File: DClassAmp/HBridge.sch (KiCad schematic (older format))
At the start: 15 parts

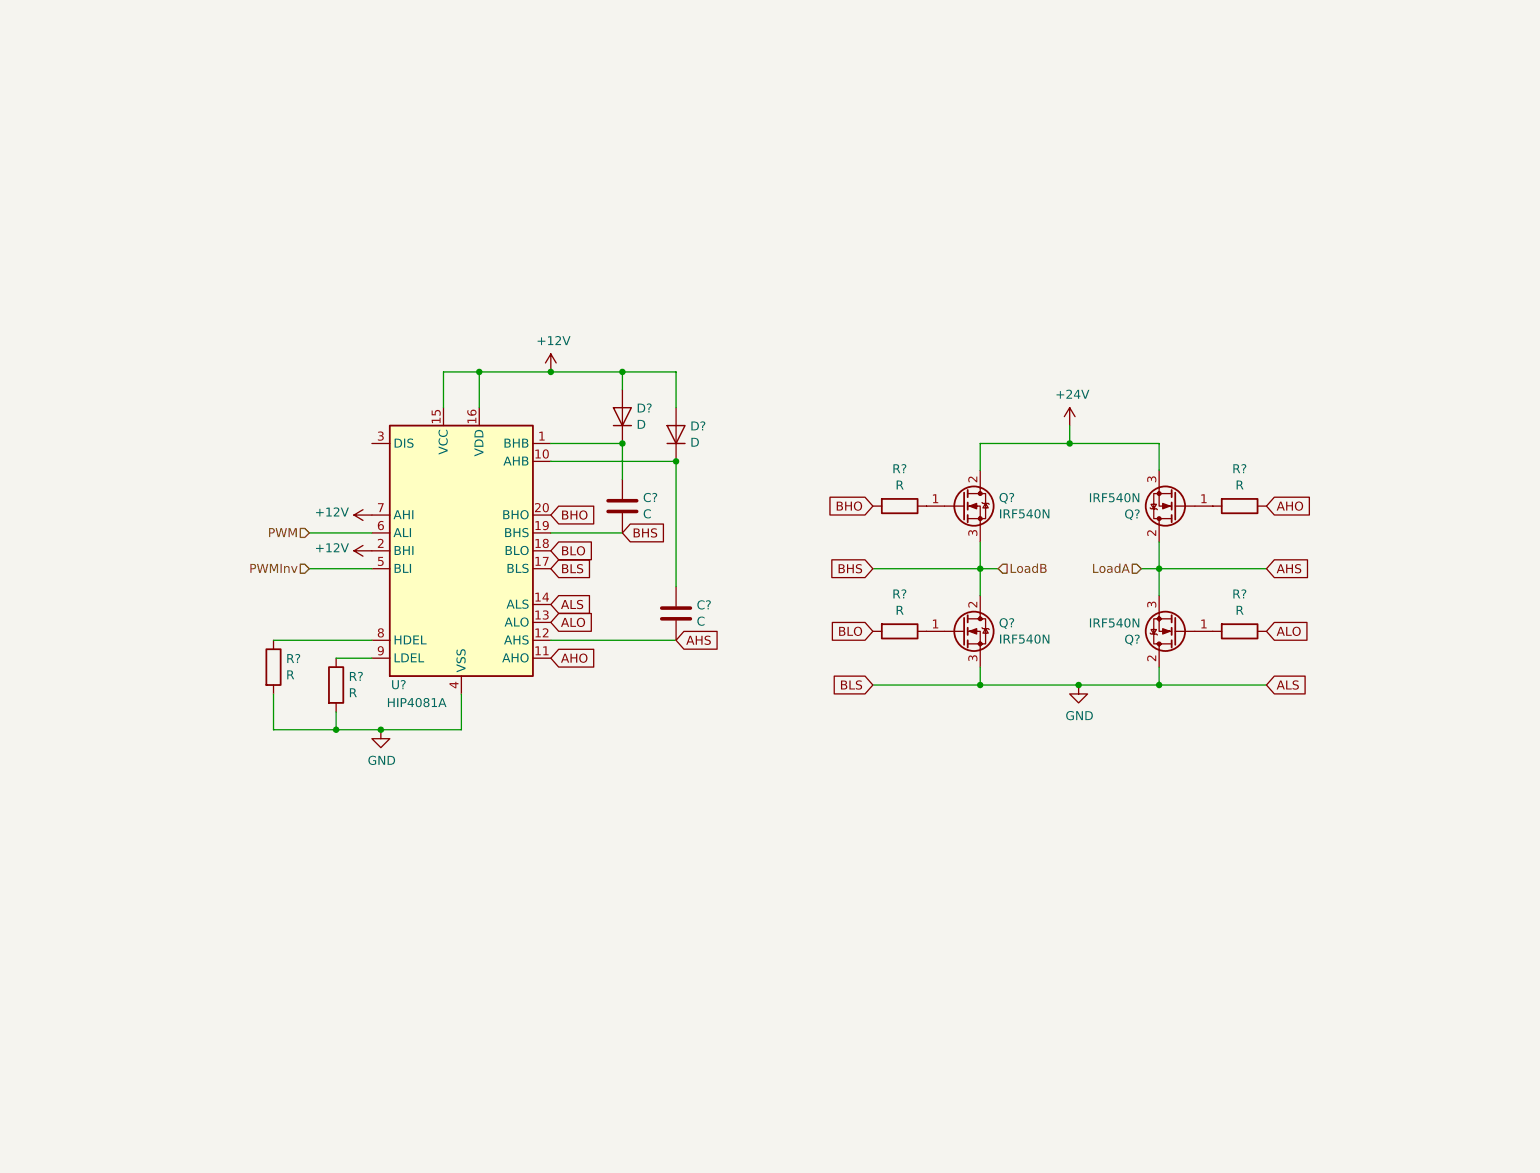
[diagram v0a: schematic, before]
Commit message: Added h bridge v2
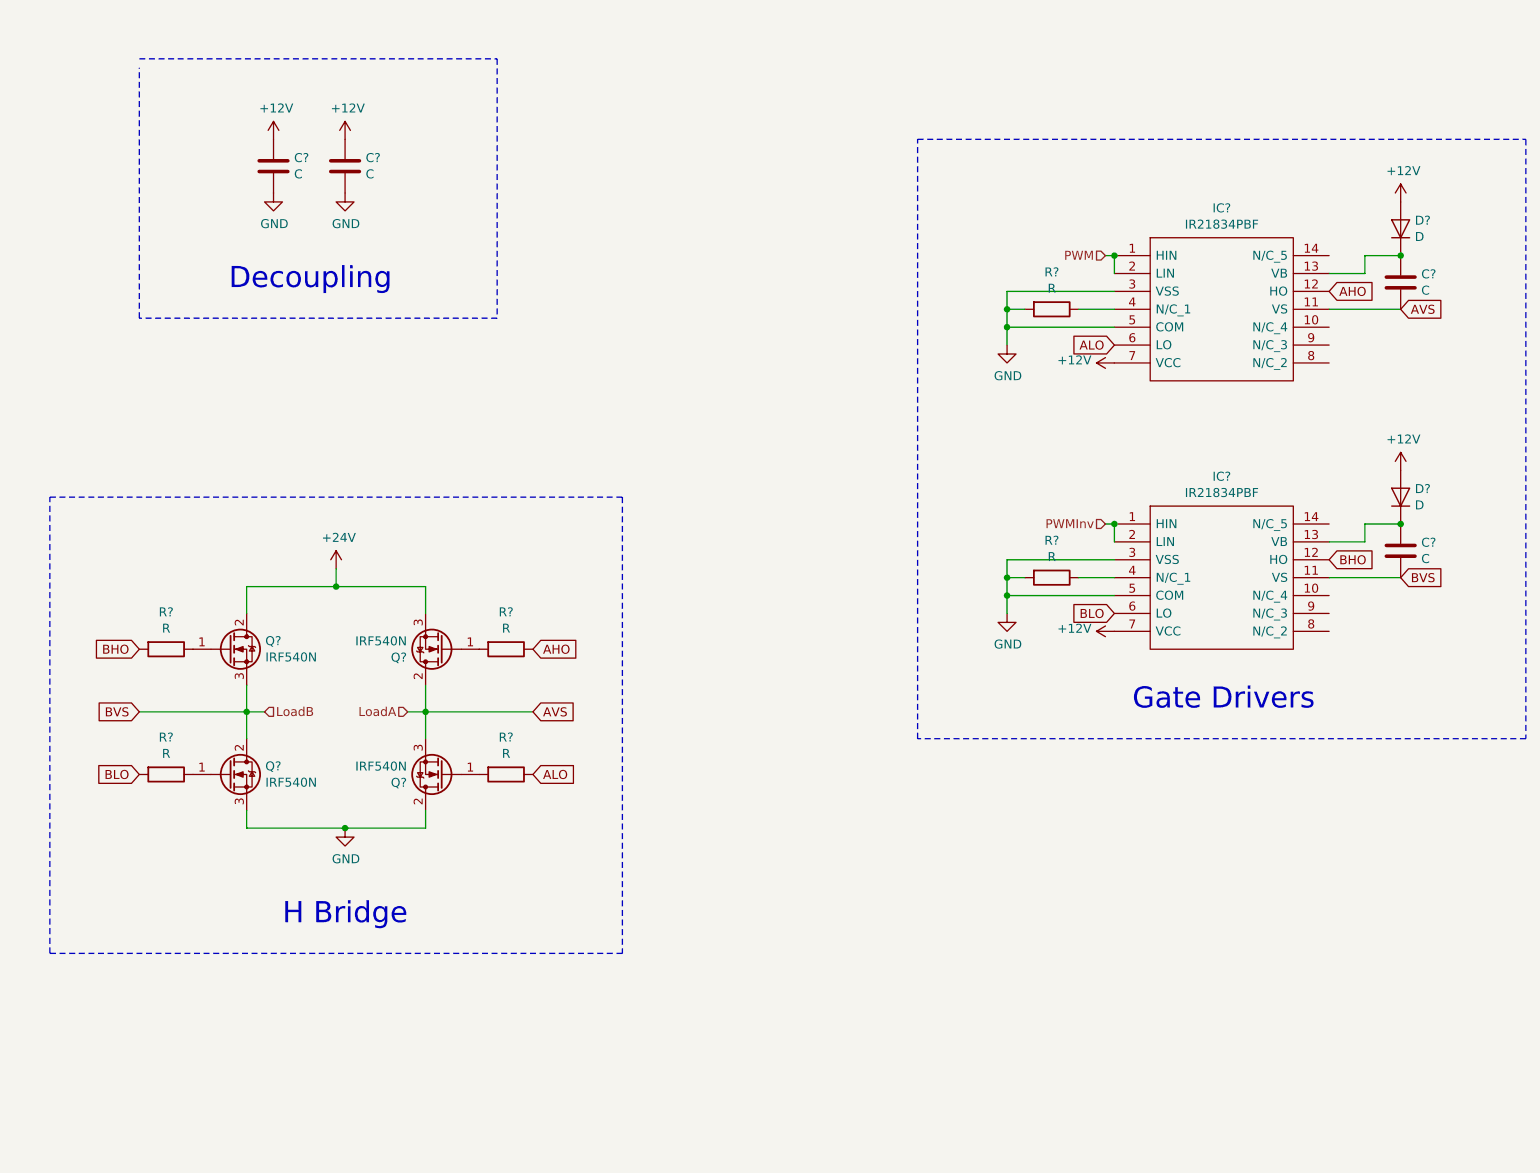
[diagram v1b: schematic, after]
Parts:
- removed C? (x2): C, symbol Device:C
- removed D? (x2): D, symbol Device:D
- removed R? (x2): R, symbol Device:R
- removed U?: HIP4081A, symbol Driver_FET:HIP4081A
- added C? (x4): C, symbol Device:C
- added D? (x2): D, symbol Device:D
- added IC? (x2): IR21834PBF, DIP762W56P254L1930H533Q14N, symbol IR21834PBF:IR21834PBF
- added R? (x2): R, symbol Device:R
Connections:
- net +12V: now also C?.1, C?.1, D?.2 (A), D?.2 (A), IC?.7 (VCC), IC?.7 (VCC)
- net AHO: now also IC?.12 (HO)
- net ALO: now also IC?.6 (LO)
- net BHO: now also IC?.12 (HO)
- net BLO: now also IC?.6 (LO)
- net GND: now also C?.2, C?.2, IC?.3 (VSS), IC?.3 (VSS), IC?.5 (COM), IC?.5 (COM), R?.2, R?.2
- net PWM: now also IC?.1 (HIN), IC?.2 (LIN)
- net PWMInv: now also IC?.1 (HIN), IC?.2 (LIN)
- net AHS renamed AVS
- net AVS: now also C?.2, IC?.11 (VS)
- net BHS renamed BVS
- net BVS: now also C?.2, IC?.11 (VS)
- new net: C?.1, D?.1 (K), IC?.13 (VB) (x2)
- new net: IC?.4 (N/C_1), R?.1 (x2)
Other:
- note added: "Decoupling"
- note added: "Gate Drivers"
- note added: "H Bridge"
- moved on the sheet: Q?, R?

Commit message: Added connector to h bridge schematic
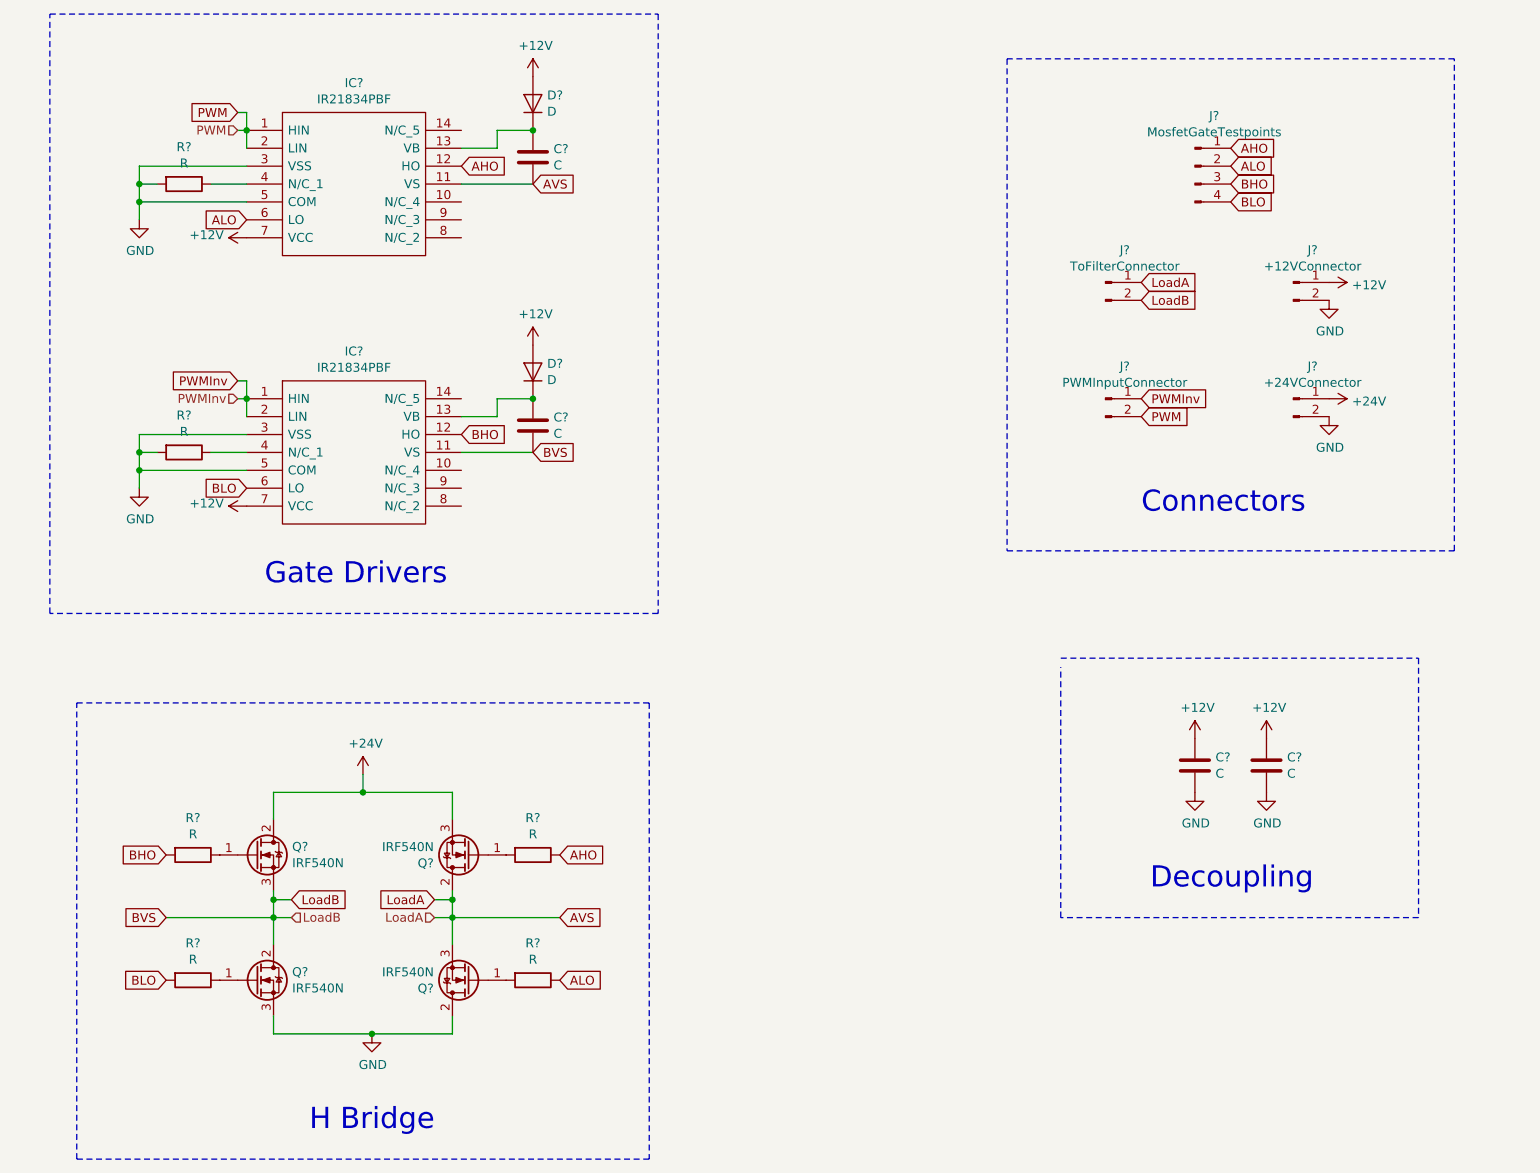
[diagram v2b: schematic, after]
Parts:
- added J?: +12VConnector, symbol Connector:Conn_01x02_Male
- added J?: +24VConnector, symbol Connector:Conn_01x02_Male
- added J?: ToFilterConnector, symbol Connector:Conn_01x02_Male
- added J?: PWMInputConnector, symbol Connector:Conn_01x02_Male
- added J?: MosfetGateTestpoints, symbol Connector:Conn_01x04_Male
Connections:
- net +12V: now also J?.1 (Pin_1)
- net +24V: now also J?.1 (Pin_1)
- net AHO: now also J?.1 (Pin_1)
- net ALO: now also J?.2 (Pin_2)
- net AVS: now also J?.1 (Pin_1)
- net BHO: now also J?.3 (Pin_3)
- net BLO: now also J?.4 (Pin_4)
- net BVS: now also J?.2 (Pin_2)
- net GND: now also J?.2 (Pin_2), J?.2 (Pin_2)
- net PWM: now also J?.2 (Pin_2)
- net PWMInv: now also J?.1 (Pin_1)
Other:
- note added: "Connectors"
- moved on the sheet: C?, D?, IC?, Q?, R?

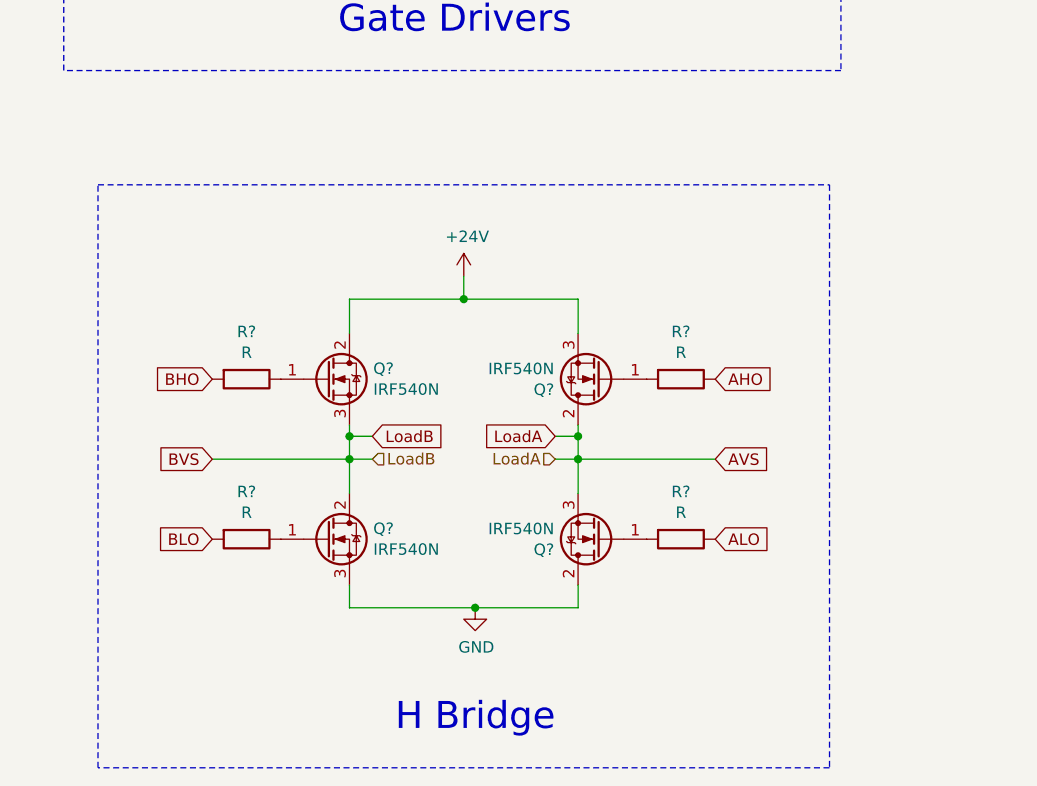
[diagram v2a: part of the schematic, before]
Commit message: Added snubber cicuit
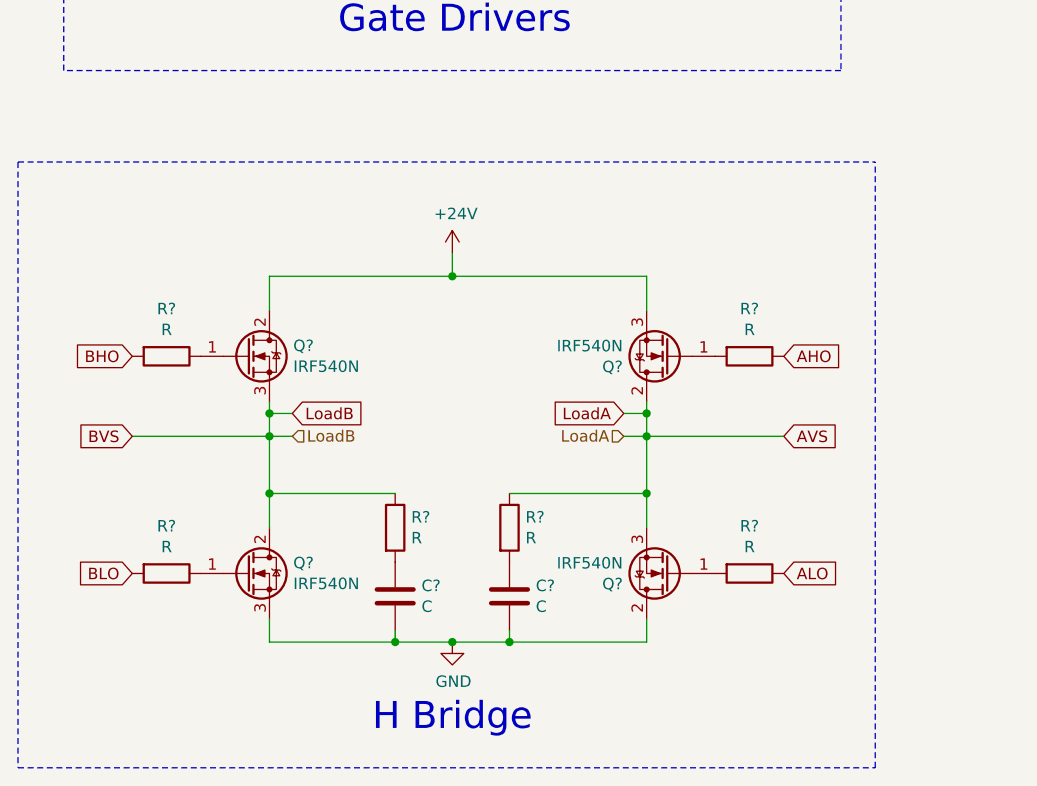
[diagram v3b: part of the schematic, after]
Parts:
- added C? (x2): C, symbol Device:C
- added R? (x2): R, symbol Device:R
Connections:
- net AVS: now also R?.1
- net BVS: now also R?.1
- net GND: now also C?.2, C?.2
- new net: C?.1, R?.2 (x2)
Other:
- moved on the sheet: Q?, R?
